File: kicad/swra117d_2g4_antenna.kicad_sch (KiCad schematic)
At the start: 2 parts, among them J1 SMA edge launch

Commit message: Retune the antenna by uniform scaling: x1.155 for the 2.83 GHz result
RFsim put this board's resonance at 2.83 GHz, 15% above the ISM band, so
the board now carries a x1.155 scaled radiator generated by the new
tools/scale_footprint.py. The published footprint stays in the library
untouched, to re-scale from.

Uniform in-plane scaling is the retune that needs no model of the meander:
scale every dimension and every gap by k and each current path and coupling
distance scales with it, so resonance moves as 1/k, k = 2.83/2.45. Scaling
also carries the feed tap and the short with it, so the input impedance is
preserved - lengthening one arm by hand would fix the frequency and break
the 50 ohm. It is first order (the substrate does not scale), so expect one
more iteration: simulate, take the ratio, rescale. ANT_SCALE and
ANT_FOOTPRINT are single constants in gen_project.py.

Supporting changes: the ground plane edge is now read from the antenna
footprint's own Dwgs.User keep-out box instead of being hardcoded, so a
rescaled antenna moves the plane with it; ANT_ORIGIN drops 0.5 mm to keep
the larger antenna clear of the board edge; the feed is 23.5 mm (TD 143 ps)
and the ngspice deck follows; the symbol points at the footprint the board
uses.

Recorded in the README what could not be established analytically: a
quarter-wave check on the arm (21.31 mm2 of copper at 0.5 mm wide -> 42.6 mm
developed, ~32.8 mm arm) needs eps_eff = 0.87 to land on 2.45 GHz and 0.65
for 2.83 GHz, both below 1. The developed length badly over-predicts the
electrical length because a meander's adjacent segments carry opposing
currents, so this geometry's resonance can only come from a field solver or
a VNA - which is why the retune uses the ratio of two frequencies rather
than a model of either.

Co-Authored-By: Claude Opus 5 <noreply@anthropic.com>
Claude-Session: https://claude.ai/code/session_01Prj6bUQ2KQzzxzD4bgtswJ
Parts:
- AE1: footprint SWRA117D_RF:Texas_SWRA117D_2.4GHz_Left -> SWRA117D_RF:SWRA117D_2G4_Left_retuned
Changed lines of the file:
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@@
 			(effects (font (size 1.27 1.27)) (justify left))
 		)
-		(property "Footprint" "SWRA117D_RF:Texas_SWRA117D_2.4GHz_Left"
+		(property "Footprint" "SWRA117D_RF:SWRA117D_2G4_Left_retuned"
 			(at 127 81.28 0)
 			(effects (font (size 1.27 1.27)) (hide yes))
 		)
 		(property "Datasheet" "~" (at 127 81.28 0) (effects (font (size 1.27 1.27)) (hide yes)))
-		(property "Description" "2.45 GHz printed inverted-F antenna (TI SWRA117D, left layout)"
+		(property "Description" "2.45 GHz printed inverted-F antenna (TI SWRA117D, left layout, geometry scaled x1.155)"
 			(at 127 81.28 0)
 			(effects (font (size 1.27 1.27)) (hide yes))

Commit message: Revert the x1.155 retune: the 2.83 GHz result came from an invalid setup
The RFsim layout plot shows the only copper in the model is the antenna, the
feed line and the connector pads - the ground pours were unfilled, so the
antenna had no ground plane. An inverted-F radiates against its plane; the
plane is half the antenna, and the 49 stitching vias connected to nothing.
The same dialog was set to RFsim's FR-4 preset, 1.6 mm / er 4.5, not this
board's 0.8 mm / er 4.4: its own 50 ohm port width guess of 3.114 mm is the
50 ohm width for 1.6 mm / er 4.5, where ours is 1.49 mm (and our 1.5 mm line
would be 71 ohm on 1.6 mm). Two large errors pulling opposite ways, so the
2.83 GHz cannot be used - and a 15% geometry change justified by it should
not stand.

ANT_SCALE is back to 1.0 on the published footprint. The scaled copy and
scale_footprint.py stay, as the retune path for when a valid run exists.

check_project.py caught its own bug while reverting: it held the ground
plane edge as a hardcoded 65.75, so once the antenna moved it reported the
board as broken. It now reads the edge from the board's copper zones, which
is where gen_project.py derives it from in the first place.

README now leads with the four settings that decide whether a run of this
board means anything: fill the zones, substrate 0.8 mm / er 4.4, domain
margin >= 31 mm (lambda/4 at 2.45 GHz, not the 4 mm default, which puts the
absorbing boundary lambda/31 from the antenna), and a port attached to the
feed line as CPW rather than Lumped with "No Line". Also a section
separating the three edges that are easy to conflate: the board edge (do not
extend it past the antenna - dielectric beside the arm loads it and pulls
resonance down), the ground plane keep-out edge (never extend copper into
it), and the simulation domain edge (this is the one to extend).

Co-Authored-By: Claude Opus 5 <noreply@anthropic.com>
Claude-Session: https://claude.ai/code/session_01Prj6bUQ2KQzzxzD4bgtswJ
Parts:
- AE1: footprint SWRA117D_RF:SWRA117D_2G4_Left_retuned -> SWRA117D_RF:Texas_SWRA117D_2.4GHz_Left
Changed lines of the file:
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@@
 			(effects (font (size 1.27 1.27)) (justify left))
 		)
-		(property "Footprint" "SWRA117D_RF:SWRA117D_2G4_Left_retuned"
+		(property "Footprint" "SWRA117D_RF:Texas_SWRA117D_2.4GHz_Left"
 			(at 127 81.28 0)
 			(effects (font (size 1.27 1.27)) (hide yes))
 		)
 		(property "Datasheet" "~" (at 127 81.28 0) (effects (font (size 1.27 1.27)) (hide yes)))
-		(property "Description" "2.45 GHz printed inverted-F antenna (TI SWRA117D, left layout, geometry scaled x1.155)"
+		(property "Description" "2.45 GHz printed inverted-F antenna (TI SWRA117D, left layout)"
 			(at 127 81.28 0)
 			(effects (font (size 1.27 1.27)) (hide yes))

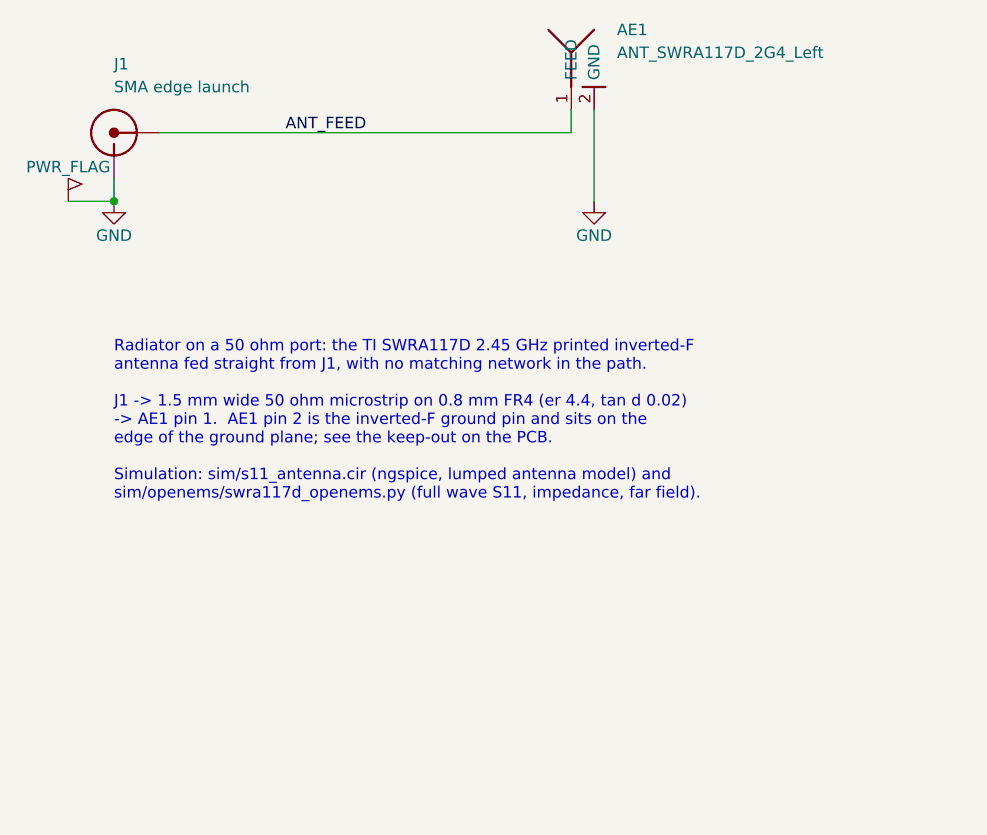
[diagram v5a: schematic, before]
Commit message: Rebuild the board for 1.6 mm FR4: the board owner says that is the stackup
The simulator was right and this project's assumption was wrong. The 0.8 mm
FR4 was picked here for a convenient line width and never verified; the
fabricated board is 1.6 mm, so the design follows the board. Stackup is now
1.6 mm / er 4.5 to match what RFsim runs.

Everything downstream is derived, so it was one constant plus a new
generator:

- 50 ohm microstrip 1.50 -> 2.95 mm (50.2 ohm)
- tools/gen_sma_footprint.py generates the connector for the stackup: signal
  pad 2.95 mm, coplanar gap 2.0 mm (launch 49.8 ohm, where the old 0.8 mm gap
  would give 45.1 ohm on this substrate), bottom ground pad 12.95 mm across
- top pour keep-away 1.0 -> 2.0 mm, and the stitching vias follow the
  connector's new pad centres

Two geometric consequences needed deciding rather than deriving. A 2.95 mm
line cannot butt against the antenna's 0.5 mm feed pad - the step would be a
real discontinuity and the wide line would crowd the antenna's ground pin at
0.175 mm - so the last 4.5 mm tapers to 0.5 mm in six stages. And the pour
corridor now starts 3 mm below the plane edge: at 2.0 mm either side it would
otherwise cut a 7 mm notch into the ground plane edge directly under the
antenna, and that edge is part of the antenna.

The antenna itself is untouched and still matches SWRA117D Table 1 exactly.
Stitching is 41 vias with a worst unstitched span of 9.1 mm (7.8 GHz).

The feed-width guard earned itself: the first attempt at this edit failed
partway, leaving a 1.5 mm line against the new 2.95 mm port pad, and the
check caught exactly that.

Co-Authored-By: Claude Opus 5 <noreply@anthropic.com>
Claude-Session: https://claude.ai/code/session_01Prj6bUQ2KQzzxzD4bgtswJ
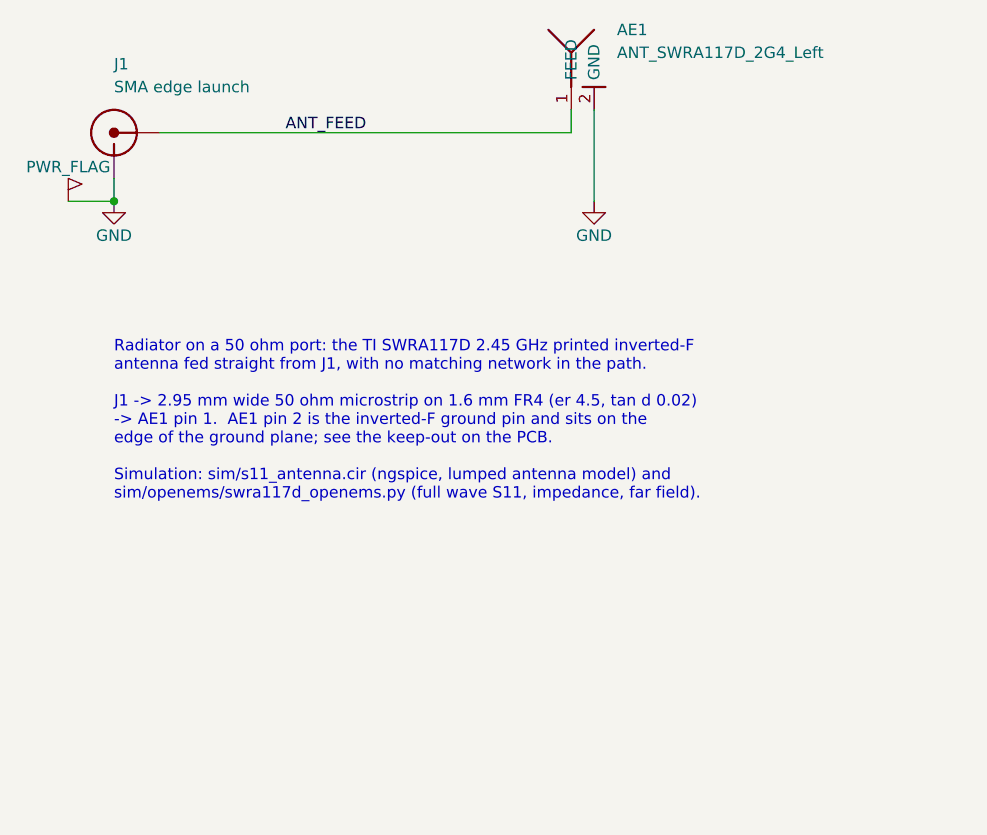
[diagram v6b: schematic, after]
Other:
- note added: "Radiator on a 50 ohm port: the TI SWRA117D 2.45 GHz printed inverted-F antenna fed straight from J1, with no matching network in the path. J1 -> 2.95 mm wide 50 ohm microstrip on 1.6 mm FR4 (er 4.5, tan d 0.02) -> AE1 pin 1. AE1 pin 2 is the inverted-F ground pin and sits on the edge of the ground plane; see the keep-out on the PCB. Simulation: sim/s11_antenna.cir (ngspice, lumped antenna model) 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"
- note removed: "Radiator on a 50 ohm port: the TI SWRA117D 2.45 GHz printed inverted-F antenna fed straight from J1, with no matching network in the path. J1 -> 1.5 mm wide 50 ohm microstrip on 0.8 mm FR4 (er 4.4, tan d 0.02) -> AE1 pin 1. AE1 pin 2 is the inverted-F ground pin and sits on the edge of the ground plane; see the keep-out on the PCB. Simulation: sim/s11_antenna.cir (ngspice, lumped antenna model) a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"
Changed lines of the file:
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@@
 		(effects (font (size 1.27 1.27)) (justify left bottom))
 	)
-	(text "Radiator on a 50 ohm port: the TI SWRA117D 2.45 GHz printed inverted-F\nantenna fed straight from J1, with no matching network in the path.\n\nJ1 -> 1.5 mm wide 50 ohm microstrip on 0.8 mm FR4 (er 4.4, tan d 0.02)\n-> AE1 pin 1.  AE1 pin 2 is the inverted-F ground pin and sits on the\nedge of the ground plane; see the keep-out on the PCB.\n\nSimulation: sim/s11_antenna.cir (ngspice, lumped antenna model) and\nsim/openems/swra117d_openems.py (full wave S11, impedance, far field)."
+	(text "Radiator on a 50 ohm port: the TI SWRA117D 2.45 GHz printed inverted-F\nantenna fed straight from J1, with no matching network in the path.\n\nJ1 -> 2.95 mm wide 50 ohm microstrip on 1.6 mm FR4 (er 4.5, tan d 0.02)\n-> AE1 pin 1.  AE1 pin 2 is the inverted-F ground pin and sits on the\nedge of the ground plane; see the keep-out on the PCB.\n\nSimulation: sim/s11_antenna.cir (ngspice, lumped antenna model) and\nsim/openems/swra117d_openems.py (full wave S11, impedance, far field)."
 		(exclude_from_sim no)
 		(at 76.2 112 0)
